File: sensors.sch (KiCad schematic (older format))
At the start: 11 parts

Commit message: Annotation
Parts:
- gave numbers to parts that had none: 11
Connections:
- net GND: no longer U4.17 (NC)
- no-connect marks 16 -> 17
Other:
- note added: "Ground distance sensor \n(Time of flight)"
- note added: "IMU 10dof"
- moved on the sheet: C19, C20, C21, C22, C23, C24, R16, R17, U4, U5, U6

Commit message: Change MCU to LQFP64 (instead of BGA)
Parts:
- added W3, W4, W5, W6, W7: TEST, symbol TEST
- U4: symbol MPU-9250 -> MPU-9250-RESCUE-speedy
- renumbered C19 to C15, C20 to C16, C21 to C17, C22 to C18, C23 to C19, C24 to C20, R16 to R15, R17 to R16
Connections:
- net MPU9250_CS: now also W6.2; no longer U4.22 (nCS)
- net MPU9250_INT: now also W7.2; no longer U4.12 (INT)
- net SPI1_MISO: now also W5.2; no longer U4.9 (AD0/SD0)
- net SPI1_MOSI: now also W4.2; no longer U4.24 (SDA/SDI)
- net SPI1_SCK: now also W3.2; no longer U4.23 (SCL/SCLK)
- net VCC: no longer C15.1, C16.1, C18.1, C19.1, C20.1, R15.1, R16.1, U4.13 (VDD), U4.8 (VDDIO), U5.1 (VDD), U5.2 (PS), U6.10 (AVDD), U6.8 (AVDD_VCSEL)
- new net: U4.12 (INT), W7.1
- new net: U4.22 (nCS), W6.1
- new net: U4.23 (SCL/SCLK), W3.1
- new net: U4.24 (SDA/SDI), W4.1
- new net: U4.9 (AD0/SD0), W5.1
- new net VCCA: C15.1, C16.1, C18.1, C19.1, C20.1, R15.1, R16.1, U4.13 (VDD), U4.8 (VDDIO), U5.1 (VDD), U5.2 (PS), U6.10 (AVDD), U6.8 (AVDD_VCSEL)
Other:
- moved on the sheet: C15, C16, C17, C18, U5

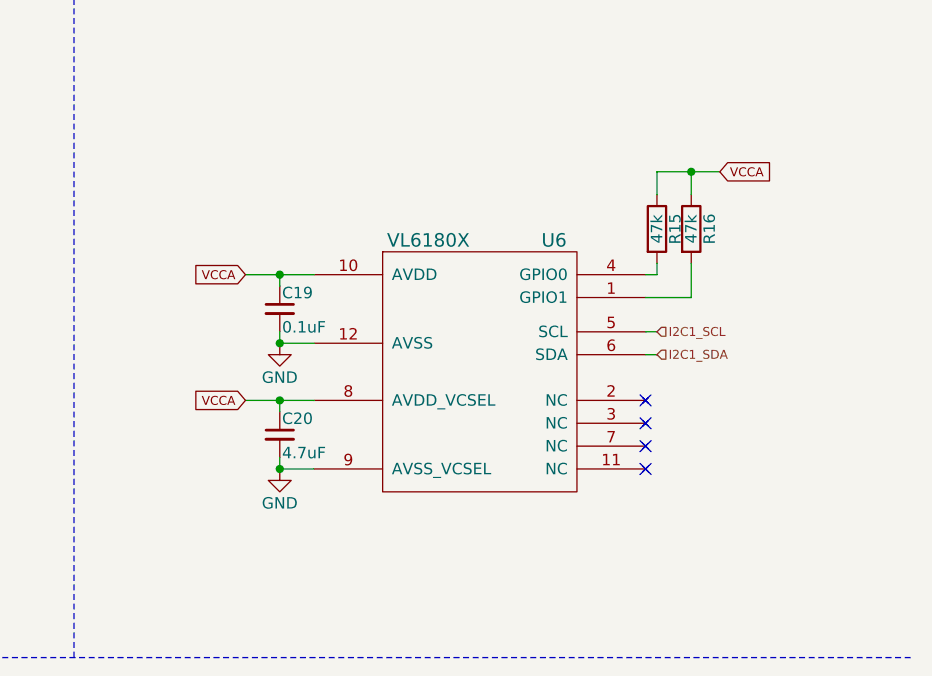
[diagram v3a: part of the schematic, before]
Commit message: Minor corrections
Wire GPIO of VL6180X to MCU
Remove UART4
Change Shottky diode
Add fuse on CAN bus power
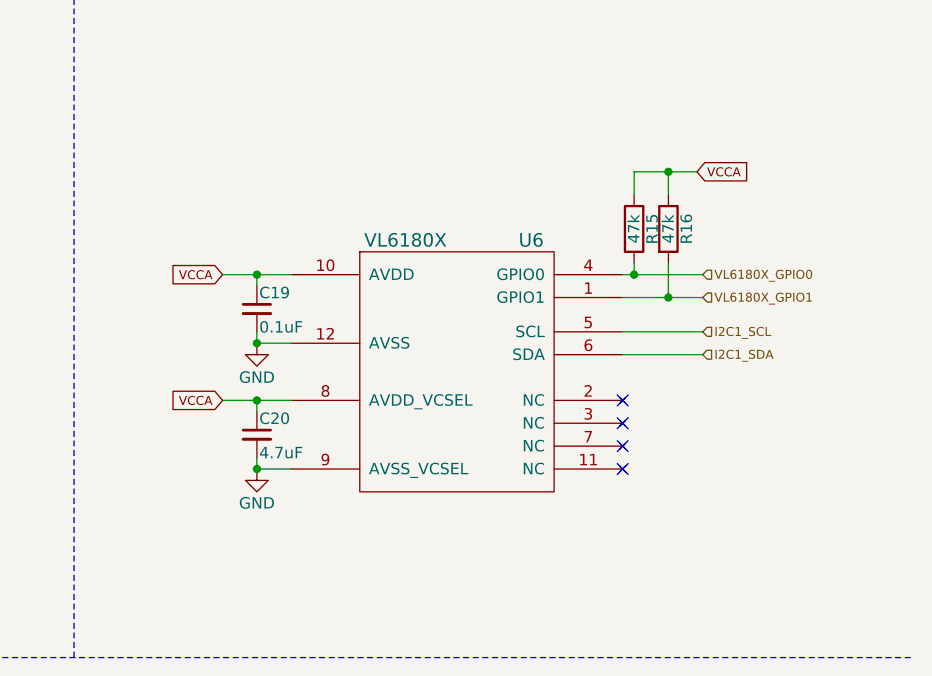
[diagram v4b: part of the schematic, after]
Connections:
- net VL6180X_GPIO0: now reaches R15.2, U6.4 (GPIO0)
- net VL6180X_GPIO1: now reaches R16.2, U6.1 (GPIO1)
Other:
- moved on the sheet: C19, C20, R15, R16, U6
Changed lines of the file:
@@
 $EndDescr
 $Comp
-L GND #PWR035
+L GND #PWR33
 U 1 1 5536D70F
 P 1275 2225
-F 0 "#PWR035" H 1275 1975 50  0001 C CNN
+F 0 "#PWR33" H 1275 1975 50  0001 C CNN
 F 1 "GND" H 1275 2075 50  0000 C CNN
 F 2 "" H 1275 2225 60  0000 C CNN
@@
 $EndComp
 $Comp
-L GND #PWR036
+L GND #PWR36
 U 1 1 5536D9F2
 P 3750 2975
-F 0 "#PWR036" H 3750 2725 50  0001 C CNN
+F 0 "#PWR36" H 3750 2725 50  0001 C CNN
 F 1 "GND" H 3750 2825 50  0000 C CNN
 F 2 "" H 3750 2975 60  0000 C CNN
@@
 NoConn ~ 3375 2875
 $Comp
-L VCC #PWR037
+L VCC #PWR34
 U 1 1 5536DF0C
 P 3525 3125
-F 0 "#PWR037" H 3525 2975 50  0001 C CNN
+F 0 "#PWR34" H 3525 2975 50  0001 C CNN
 F 1 "VCC" H 3525 3275 50  0000 C CNN
 F 2 "" H 3525 3125 60  0000 C CNN
@@
 $EndComp
 $Comp
-L GND #PWR038
+L GND #PWR35
 U 1 1 5536DF1F
 P 3525 3225
-F 0 "#PWR038" H 3525 2975 50  0001 C CNN
+F 0 "#PWR35" H 3525 2975 50  0001 C CNN
 F 1 "GND" H 3525 3075 50  0000 C CNN
 F 2 "" H 3525 3225 60  0000 C CNN
@@
 $EndComp
 $Comp
-L GND #PWR039
+L GND #PWR40
 U 1 1 5536FBED
-P 8450 3250
-F 0 "#PWR039" H 8450 3000 50  0001 C CNN
-F 1 "GND" H 8450 3100 50  0000 C CNN
-F 2 "" H 8450 3250 60  0000 C CNN
-F 3 "" H 8450 3250 60  0000 C CNN
-	1    8450 3250
-	1    0    0    -1
-$EndComp
-$Comp
-L GND #PWR040
+P 8350 3250
+F 0 "#PWR40" H 8350 3000 50  0001 C CNN
+F 1 "GND" H 8350 3100 50  0000 C CNN
+F 2 "" H 8350 3250 60  0000 C CNN
+F 3 "" H 8350 3250 60  0000 C CNN
+	1    8350 3250
+	1    0    0    -1
+$EndComp
+$Comp
+L GND #PWR39
 U 1 1 5536FC2A
-P 8450 2700
-F 0 "#PWR040" H 8450 2450 50  0001 C CNN
-F 1 "GND" H 8450 2550 50  0000 C CNN
-F 2 "" H 8450 2700 60  0000 C CNN
-F 3 "" H 8450 2700 60  0000 C CNN
-	1    8450 2700
+P 8350 2700
+F 0 "#PWR39" H 8350 2450 50  0001 C CNN
+F 1 "GND" H 8350 2550 50  0000 C CNN
+F 2 "" H 8350 2700 60  0000 C CNN
+F 3 "" H 8350 2700 60  0000 C CNN
+	1    8350 2700
 	1    0    0    -1
 $EndComp
@@
 L R R15
 U 1 1 5536FCF9
-P 10100 2200
-F 0 "R15" V 10180 2200 50  0000 C CNN
-F 1 "47k" V 10100 2200 50  0000 C CNN
-F 2 "" V 10030 2200 30  0000 C CNN
-F 3 "" H 10100 2200 30  0000 C CNN
-	1    10100 2200
+P 10000 2200
+F 0 "R15" V 10080 2200 50  0000 C CNN
+F 1 "47k" V 10000 2200 50  0000 C CNN
+F 2 "" V 9930 2200 30  0000 C CNN
+F 3 "" H 10000 2200 30  0000 C CNN
+	1    10000 2200
 	1    0    0    -1
 $EndComp
@@
 L R R16
 U 1 1 5536FD36
-P 10250 2200
-F 0 "R16" V 10330 2200 50  0000 C CNN
-F 1 "47k" V 10250 2200 50  0000 C CNN
-F 2 "" V 10180 2200 30  0000 C CNN
-F 3 "" H 10250 2200 30  0000 C CNN
-	1    10250 2200
+P 10150 2200
+F 0 "R16" V 10230 2200 50  0000 C CNN
+F 1 "47k" V 10150 2200 50  0000 C CNN
+F 2 "" V 10080 2200 30  0000 C CNN
+F 3 "" H 10150 2200 30  0000 C CNN
+	1    10150 2200
 	1    0    0    -1
 $EndComp
@@
 L VL6180X U6
 U 1 1 553709E6
-P 9000 2650
-F 0 "U6" H 9650 3050 59  0000 C CNN
-F 1 "VL6180X" H 9100 3050 59  0000 C CNN
-F 2 "" H 9200 3250 39  0000 C CNN
-F 3 "" H 9200 3250 39  0000 C CNN
-	1    9000 2650
+P 8900 2650
+F 0 "U6" H 9550 3050 59  0000 C CNN
+F 1 "VL6180X" H 9000 3050 59  0000 C CNN
+F 2 "" H 9100 3250 39  0000 C CNN
+F 3 "" H 9100 3250 39  0000 C CNN
+	1    8900 2650
 	1    0    0    -1
 $EndComp
@@
 $EndComp
 $Comp
-L GND #PWR041
+L GND #PWR37
 U 1 1 553864F8
 P 4975 2750
-F 0 "#PWR041" H 4975 2500 50  0001 C CNN
+F 0 "#PWR37" H 4975 2500 50  0001 C CNN
 F 1 "GND" H 4975 2600 50  0000 C CNN
 F 2 "" H 4975 2750 60  0000 C CNN
@@
 NoConn ~ 6725 2525
 $Comp
-L GND #PWR042
+L GND #PWR38
 U 1 1 55386A50
 P 6775 2775
-F 0 "#PWR042" H 6775 2525 50  0001 C CNN
+F 0 "#PWR38" H 6775 2525 50  0001 C CNN
 F 1 "GND" H 6775 2625 50  0000 C CNN
 F 2 "" H 6775 2775 60  0000 C CNN
@@
 	1    0    0    -1
 $EndComp
-NoConn ~ 10050 2950
-NoConn ~ 10050 3050
-NoConn ~ 10050 3150
-NoConn ~ 10050 3250
+NoConn ~ 9950 2950
+NoConn ~ 9950 3050
+NoConn ~ 9950 3150
+NoConn ~ 9950 3250
 NoConn ~ 1775 3125
 NoConn ~ 1775 3025
@@
 L C_Small C19
 U 1 1 55429127
-P 8450 2550
-F 0 "C19" H 8460 2620 50  0000 L CNN
-F 1 "0.1uF" H 8460 2470 50  0000 L CNN
-F 2 "" H 8450 2550 60  0000 C CNN
-F 3 "" H 8450 2550 60  0000 C CNN
-	1    8450 2550
+P 8350 2550
+F 0 "C19" H 8360 2620 50  0000 L CNN
+F 1 "0.1uF" H 8360 2470 50  0000 L CNN
+F 2 "" H 8350 2550 60  0000 C CNN
+F 3 "" H 8350 2550 60  0000 C CNN
+	1    8350 2550
 	1    0    0    -1
 $EndComp
@@
 L C_Small C20
 U 1 1 55429407
-P 8450 3100
-F 0 "C20" H 8460 3170 50  0000 L CNN
-F 1 "4.7uF" H 8460 3020 50  0000 L CNN
-F 2 "" H 8450 3100 60  0000 C CNN
-F 3 "" H 8450 3100 60  0000 C CNN
-	1    8450 3100
+P 8350 3100
+F 0 "C20" H 8360 3170 50  0000 L CNN
+F 1 "4.7uF" H 8360 3020 50  0000 L CNN
+F 2 "" H 8350 3100 60  0000 C CNN
+F 3 "" H 8350 3100 60  0000 C CNN
+	1    8350 3100
 	1    0    0    -1
 $EndComp
@@
 	3375 3125 3525 3125
 Wire Wire Line
-	8300 2950 8600 2950
-Wire Wire Line
-	8450 3250 8600 3250
-Connection ~ 8450 3250
-Connection ~ 8450 2950
-Wire Wire Line
-	10100 1950 10375 1950
-Wire Wire Line
-	10250 1950 10250 2050
-Wire Wire Line
-	10100 1950 10100 2050
-Connection ~ 10250 1950
-Wire Wire Line
-	10050 2400 10100 2400
-Wire Wire Line
-	10050 2500 10250 2500
-Wire Wire Line
-	10250 2500 10250 2350
-Wire Wire Line
-	10050 2650 10100 2650
-Wire Wire Line
-	10050 2750 10100 2750
-Wire Wire Line
-	10100 2400 10100 2350
-Wire Wire Line
-	8300 2400 8600 2400
+	8200 2950 8500 2950
+Wire Wire Line
+	8350 3250 8500 3250
+Connection ~ 8350 3250
+Connection ~ 8350 2950
+Wire Wire Line
+	10000 1950 10275 1950
+Wire Wire Line
+	10150 1950 10150 2050
+Wire Wire Line
+	10000 1950 10000 2050
+Connection ~ 10150 1950
+Wire Wire Line
+	9950 2400 10300 2400
+Wire Wire Line
+	9950 2500 10300 2500
+Wire Wire Line
+	10150 2500 10150 2350
+Wire Wire Line
+	9950 2650 10300 2650
+Wire Wire Line
+	9950 2750 10300 2750
+Wire Wire Line
+	10000 2400 10000 2350
+Wire Wire Line
+	8200 2400 8500 2400
 Wire Wire Line
 	4975 2675 4975 2750
@@
 Connection ~ 5175 2425
 Wire Wire Line
-	8600 2700 8450 2700
-Wire Wire Line
-	8450 2700 8450 2650
-Wire Wire Line
-	8450 2400 8450 2450
-Connection ~ 8450 2400
-Connection ~ 8450 2700
-Wire Wire Line
-	8450 3000 8450 2950
-Wire Wire Line
-	8450 3200 8450 3250
+	8500 2700 8350 2700
+Wire Wire Line
+	8350 2700 8350 2650
+Wire Wire Line
+	8350 2400 8350 2450
+Connection ~ 8350 2400
+Connection ~ 8350 2700
+Wire Wire Line
+	8350 3000 8350 2950
+Wire Wire Line
+	8350 3200 8350 3250
 Wire Notes Line
 	7550 4075 7550 500
@@
 Text HLabel 6775 2425 2    39   Input ~ 0
 I2C1_SDA
-Text HLabel 10100 2650 2    39   Input ~ 0
+Text HLabel 10300 2650 2    39   Input ~ 0
 I2C1_SCL
-Text HLabel 10100 2750 2    39   Input ~ 0
+Text HLabel 10300 2750 2    39   Input ~ 0
 I2C1_SDA
 NoConn ~ 1775 3225
@@
 Text GLabel 4975 2275 0    39   Input ~ 0
 VCCA
-Text GLabel 8300 2400 0    39   Input ~ 0
+Text GLabel 8200 2400 0    39   Input ~ 0
 VCCA
-Text GLabel 8300 2950 0    39   Input ~ 0
+Text GLabel 8200 2950 0    39   Input ~ 0
 VCCA
-Text GLabel 10375 1950 2    39   Input ~ 0
+Text GLabel 10275 1950 2    39   Input ~ 0
 VCCA
 $Comp
@@
 Wire Notes Line
 	475  4075 11225 4075
+Text HLabel 10300 2500 2    39   Input ~ 0
+VL6180X_GPIO1
+Text HLabel 10300 2400 2    39   Input ~ 0
+VL6180X_GPIO0
+Connection ~ 10000 2400
+Connection ~ 10150 2500
 $EndSCHEMATC

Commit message: Netlist
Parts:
- C15, C16, C17, C18, C19, C20, R15, R16: footprint (none) -> _std:_0402
- U4: footprint (none) -> Housings_DFN_QFN:QFN-24-1EP_3x3mm_Pitch0.4mm
- U5: footprint MODULE -> _sensors:_MS5611-01BA
- U6: footprint (none) -> _sensors:VL6180X
- W3, W4, W5, W6, W7: footprint (none) -> Measurement_Points:Measurement_Point_Square-SMD-Pad_Small
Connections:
- net VL6180X_GPIO0: no longer names the net of R15.2, U6.4 (GPIO0)
- net VL6180X_GPIO1: no longer names the net of R16.2, U6.1 (GPIO1)
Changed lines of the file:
@@
 $EndDescr
 $Comp
-L GND #PWR33
+L GND #PWR033
 U 1 1 5536D70F
 P 1275 2225
-F 0 "#PWR33" H 1275 1975 50  0001 C CNN
+F 0 "#PWR033" H 1275 1975 50  0001 C CNN
 F 1 "GND" H 1275 2075 50  0000 C CNN
 F 2 "" H 1275 2225 60  0000 C CNN
@@
 $EndComp
 $Comp
-L GND #PWR36
+L GND #PWR034
 U 1 1 5536D9F2
 P 3750 2975
-F 0 "#PWR36" H 3750 2725 50  0001 C CNN
+F 0 "#PWR034" H 3750 2725 50  0001 C CNN
 F 1 "GND" H 3750 2825 50  0000 C CNN
 F 2 "" H 3750 2975 60  0000 C CNN
@@
 NoConn ~ 3375 2875
 $Comp
-L VCC #PWR34
+L VCC #PWR035
 U 1 1 5536DF0C
 P 3525 3125
-F 0 "#PWR34" H 3525 2975 50  0001 C CNN
+F 0 "#PWR035" H 3525 2975 50  0001 C CNN
 F 1 "VCC" H 3525 3275 50  0000 C CNN
 F 2 "" H 3525 3125 60  0000 C CNN
@@
 $EndComp
 $Comp
-L GND #PWR35
+L GND #PWR036
 U 1 1 5536DF1F
 P 3525 3225
-F 0 "#PWR35" H 3525 2975 50  0001 C CNN
+F 0 "#PWR036" H 3525 2975 50  0001 C CNN
 F 1 "GND" H 3525 3075 50  0000 C CNN
 F 2 "" H 3525 3225 60  0000 C CNN
@@
 $EndComp
 $Comp
-L GND #PWR40
+L GND #PWR037
 U 1 1 5536FBED
 P 8350 3250
-F 0 "#PWR40" H 8350 3000 50  0001 C CNN
+F 0 "#PWR037" H 8350 3000 50  0001 C CNN
 F 1 "GND" H 8350 3100 50  0000 C CNN
 F 2 "" H 8350 3250 60  0000 C CNN
@@
 $EndComp
 $Comp
-L GND #PWR39
+L GND #PWR038
 U 1 1 5536FC2A
 P 8350 2700
-F 0 "#PWR39" H 8350 2450 50  0001 C CNN
+F 0 "#PWR038" H 8350 2450 50  0001 C CNN
 F 1 "GND" H 8350 2550 50  0000 C CNN
 F 2 "" H 8350 2700 60  0000 C CNN
@@
 F 0 "R15" V 10080 2200 50  0000 C CNN
 F 1 "47k" V 10000 2200 50  0000 C CNN
-F 2 "" V 9930 2200 30  0000 C CNN
+F 2 "_std:_0402" V 9930 2200 30  0001 C CNN
 F 3 "" H 10000 2200 30  0000 C CNN
 	1    10000 2200
@@
 F 0 "R16" V 10230 2200 50  0000 C CNN
 F 1 "47k" V 10150 2200 50  0000 C CNN
-F 2 "" V 10080 2200 30  0000 C CNN
+F 2 "_std:_0402" V 10080 2200 30  0001 C CNN
 F 3 "" H 10150 2200 30  0000 C CNN
 	1    10150 2200
@@
 F 0 "U6" H 9550 3050 59  0000 C CNN
 F 1 "VL6180X" H 9000 3050 59  0000 C CNN
-F 2 "" H 9100 3250 39  0000 C CNN
+F 2 "_sensors:VL6180X" H 9100 3250 39  0001 C CNN
 F 3 "" H 9100 3250 39  0000 C CNN
 	1    8900 2650
@@
 F 0 "U5" H 6325 2925 50  0000 C CNN
 F 1 "MS5611-01BA" H 5825 2925 50  0000 C CNN
-F 2 "MODULE" H 5975 2525 50  0001 C CNN
+F 2 "_sensors:_MS5611-01BA" H 5975 2525 50  0001 C CNN
 F 3 "DOCUMENTATION" H 5975 2525 50  0001 C CNN
 	1    5975 2525
@@
 $EndComp
 $Comp
-L GND #PWR37
+L GND #PWR039
 U 1 1 553864F8
 P 4975 2750
-F 0 "#PWR37" H 4975 2500 50  0001 C CNN
+F 0 "#PWR039" H 4975 2500 50  0001 C CNN
 F 1 "GND" H 4975 2600 50  0000 C CNN
 F 2 "" H 4975 2750 60  0000 C CNN
@@
 NoConn ~ 6725 2525
 $Comp
-L GND #PWR38
+L GND #PWR040
 U 1 1 55386A50
 P 6775 2775
-F 0 "#PWR38" H 6775 2525 50  0001 C CNN
+F 0 "#PWR040" H 6775 2525 50  0001 C CNN
 F 1 "GND" H 6775 2625 50  0000 C CNN
 F 2 "" H 6775 2775 60  0000 C CNN
@@
 F 0 "U4" H 2975 3325 60  0000 C CNN
 F 1 "MPU-9250" H 2325 3325 60  0000 C CNN
-F 2 "" H 2575 3125 60  0000 C CNN
+F 2 "Housings_DFN_QFN:QFN-24-1EP_3x3mm_Pitch0.4mm" H 2575 3125 60  0001 C CNN
 F 3 "" H 2575 3125 60  0000 C CNN
 	1    2575 2525
@@
 F 0 "C15" H 1285 2095 50  0000 L CNN
 F 1 "0.1uF" H 1285 1945 50  0000 L CNN
-F 2 "" H 1275 2025 60  0000 C CNN
+F 2 "_std:_0402" H 1275 2025 60  0001 C CNN
 F 3 "" H 1275 2025 60  0000 C CNN
 	1    1275 2025
@@
 F 0 "C16" H 1535 2095 50  0000 L CNN
 F 1 "10nF" H 1535 1945 50  0000 L CNN
-F 2 "" H 1525 2025 60  0000 C CNN
+F 2 "_std:_0402" H 1525 2025 60  0001 C CNN
 F 3 "" H 1525 2025 60  0000 C CNN
 	1    1525 2025
@@
 F 0 "C17" H 3760 2945 50  0000 L CNN
 F 1 "0.1uF" H 3760 2795 50  0000 L CNN
-F 2 "" H 3750 2875 60  0000 C CNN
+F 2 "_std:_0402" H 3750 2875 60  0001 C CNN
 F 3 "" H 3750 2875 60  0000 C CNN
 	1    3750 2875
@@
 F 0 "C18" H 4985 2645 50  0000 L CNN
 F 1 "0.1uF" H 4985 2495 50  0000 L CNN
-F 2 "" H 4975 2575 60  0000 C CNN
+F 2 "_std:_0402" H 4975 2575 60  0001 C CNN
 F 3 "" H 4975 2575 60  0000 C CNN
 	1    4975 2575
@@
 F 0 "C19" H 8360 2620 50  0000 L CNN
 F 1 "0.1uF" H 8360 2470 50  0000 L CNN
-F 2 "" H 8350 2550 60  0000 C CNN
+F 2 "_std:_0402" H 8350 2550 60  0001 C CNN
 F 3 "" H 8350 2550 60  0000 C CNN
 	1    8350 2550
@@
 F 0 "C20" H 8360 3170 50  0000 L CNN
 F 1 "4.7uF" H 8360 3020 50  0000 L CNN
-F 2 "" H 8350 3100 60  0000 C CNN
+F 2 "_std:_0402" H 8350 3100 60  0001 C CNN
 F 3 "" H 8350 3100 60  0000 C CNN
 	1    8350 3100
@@
 	10000 1950 10000 2050
 Connection ~ 10150 1950
-Wire Wire Line
-	9950 2400 10300 2400
-Wire Wire Line
-	9950 2500 10300 2500
 Wire Wire Line
 	10150 2500 10150 2350
@@
 F 0 "W3" H 3725 2150 40  0000 C CNN
 F 1 "TEST" H 3575 2125 20  0000 C CNN
-F 2 "" H 3575 2125 60  0000 C CNN
+F 2 "Measurement_Points:Measurement_Point_Square-SMD-Pad_Small" H 3575 2125 60  0001 C CNN
 F 3 "" H 3575 2125 60  0000 C CNN
 	1    3575 2125
@@
 F 0 "W4" H 3725 2250 40  0000 C CNN
 F 1 "TEST" H 3575 2225 20  0000 C CNN
-F 2 "" H 3575 2225 60  0000 C CNN
+F 2 "Measurement_Points:Measurement_Point_Square-SMD-Pad_Small" H 3575 2225 60  0001 C CNN
 F 3 "" H 3575 2225 60  0000 C CNN
 	1    3575 2225
@@
 F 0 "W5" H 3725 2400 40  0000 C CNN
 F 1 "TEST" H 3575 2375 20  0000 C CNN
-F 2 "" H 3575 2375 60  0000 C CNN
+F 2 "Measurement_Points:Measurement_Point_Square-SMD-Pad_Small" H 3575 2375 60  0001 C CNN
 F 3 "" H 3575 2375 60  0000 C CNN
 	1    3575 2375
@@
 F 0 "W6" H 3725 2550 40  0000 C CNN
 F 1 "TEST" H 3575 2525 20  0000 C CNN
-F 2 "" H 3575 2525 60  0000 C CNN
+F 2 "Measurement_Points:Measurement_Point_Square-SMD-Pad_Small" H 3575 2525 60  0001 C CNN
 F 3 "" H 3575 2525 60  0000 C CNN
 	1    3575 2525
@@
 F 0 "W7" H 3725 2700 40  0000 C CNN
 F 1 "TEST" H 3575 2675 20  0000 C CNN
-F 2 "" H 3575 2675 60  0000 C CNN
+F 2 "Measurement_Points:Measurement_Point_Square-SMD-Pad_Small" H 3575 2675 60  0001 C CNN
 F 3 "" H 3575 2675 60  0000 C CNN
 	1    3575 2675
@@
 Wire Notes Line
 	475  4075 11225 4075
-Text HLabel 10300 2500 2    39   Input ~ 0
-VL6180X_GPIO1
-Text HLabel 10300 2400 2    39   Input ~ 0
-VL6180X_GPIO0
-Connection ~ 10000 2400
-Connection ~ 10150 2500
+Wire Wire Line
+	9950 2400 10000 2400
+Wire Wire Line
+	9950 2500 10150 2500
 $EndSCHEMATC

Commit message: Remove CAN interface
(not useful enough, takes too much place)
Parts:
- W3, W4, W5, W6, W7: footprint Measurement_Points:Measurement_Point_Square-SMD-Pad_Small -> _std:Measurement_Point_Round-SMD-Pad_Small
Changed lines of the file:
@@
 F 0 "W3" H 3725 2150 40  0000 C CNN
 F 1 "TEST" H 3575 2125 20  0000 C CNN
-F 2 "Measurement_Points:Measurement_Point_Square-SMD-Pad_Small" H 3575 2125 60  0001 C CNN
+F 2 "_std:Measurement_Point_Round-SMD-Pad_Small" H 3575 2125 60  0001 C CNN
 F 3 "" H 3575 2125 60  0000 C CNN
 	1    3575 2125
@@
 F 0 "W4" H 3725 2250 40  0000 C CNN
 F 1 "TEST" H 3575 2225 20  0000 C CNN
-F 2 "Measurement_Points:Measurement_Point_Square-SMD-Pad_Small" H 3575 2225 60  0001 C CNN
+F 2 "_std:Measurement_Point_Round-SMD-Pad_Small" H 3575 2225 60  0001 C CNN
 F 3 "" H 3575 2225 60  0000 C CNN
 	1    3575 2225
@@
 F 0 "W5" H 3725 2400 40  0000 C CNN
 F 1 "TEST" H 3575 2375 20  0000 C CNN
-F 2 "Measurement_Points:Measurement_Point_Square-SMD-Pad_Small" H 3575 2375 60  0001 C CNN
+F 2 "_std:Measurement_Point_Round-SMD-Pad_Small" H 3575 2375 60  0001 C CNN
 F 3 "" H 3575 2375 60  0000 C CNN
 	1    3575 2375
@@
 F 0 "W6" H 3725 2550 40  0000 C CNN
 F 1 "TEST" H 3575 2525 20  0000 C CNN
-F 2 "Measurement_Points:Measurement_Point_Square-SMD-Pad_Small" H 3575 2525 60  0001 C CNN
+F 2 "_std:Measurement_Point_Round-SMD-Pad_Small" H 3575 2525 60  0001 C CNN
 F 3 "" H 3575 2525 60  0000 C CNN
 	1    3575 2525
@@
 F 0 "W7" H 3725 2700 40  0000 C CNN
 F 1 "TEST" H 3575 2675 20  0000 C CNN
-F 2 "Measurement_Points:Measurement_Point_Square-SMD-Pad_Small" H 3575 2675 60  0001 C CNN
+F 2 "_std:Measurement_Point_Round-SMD-Pad_Small" H 3575 2675 60  0001 C CNN
 F 3 "" H 3575 2675 60  0000 C CNN
 	1    3575 2675

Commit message: Regenerate netlist & Start placing footprints
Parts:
- removed W3, W4, W5, W6, W7: TEST, _std:Measurement_Point_Round-SMD-Pad_Small, symbol TEST
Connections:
- net MPU9250_CS: now also U4.22 (nCS)
- net MPU9250_INT: now also U4.12 (INT)
- net SPI1_MISO: now also U4.9 (AD0/SD0)
- net SPI1_MOSI: now also U4.24 (SDA/SDI)
- net SPI1_SCK: now also U4.23 (SCL/SCLK)
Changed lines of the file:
@@
 EESchema Schematic File Version 2
-LIBS:speedy-rescue
 LIBS:speedy-cache
 LIBS:power
@@
 	1    0    0    -1
 $EndComp
-Text HLabel 3825 2125 2    39   Input ~ 0
+Text HLabel 3425 2125 2    39   Input ~ 0
 SPI1_SCK
-Text HLabel 3825 2225 2    39   Input ~ 0
+Text HLabel 3425 2225 2    39   Input ~ 0
 SPI1_MOSI
-Text HLabel 3825 2375 2    39   Input ~ 0
+Text HLabel 3425 2375 2    39   Input ~ 0
 SPI1_MISO
-Text HLabel 3825 2525 2    39   Input ~ 0
+Text HLabel 3425 2525 2    39   Input ~ 0
 MPU9250_CS
-Text HLabel 3825 2675 2    39   Input ~ 0
+Text HLabel 3425 2675 2    39   Input ~ 0
 MPU9250_INT
 $Comp
@@
 	3750 2775 3375 2775
 Wire Wire Line
-	3825 2375 3775 2375
-Wire Wire Line
-	3825 2525 3775 2525
-Wire Wire Line
-	3825 2225 3775 2225
-Wire Wire Line
-	3825 2125 3775 2125
-Wire Wire Line
-	3825 2675 3775 2675
+	3425 2375 3375 2375
+Wire Wire Line
+	3425 2525 3375 2525
+Wire Wire Line
+	3425 2225 3375 2225
+Wire Wire Line
+	3425 2125 3375 2125
+Wire Wire Line
+	3425 2675 3375 2675
 Wire Wire Line
 	3525 3225 3375 3225
@@
 Text GLabel 10275 1950 2    39   Input ~ 0
 VCCA
-$Comp
-L TEST W3
-U 1 1 55799AAF
-P 3575 2125
-F 0 "W3" H 3725 2150 40  0000 C CNN
-F 1 "TEST" H 3575 2125 20  0000 C CNN
-F 2 "_std:Measurement_Point_Round-SMD-Pad_Small" H 3575 2125 60  0001 C CNN
-F 3 "" H 3575 2125 60  0000 C CNN
-	1    3575 2125
-	1    0    0    -1
-$EndComp
-$Comp
-L TEST W4
-U 1 1 55799BD9
-P 3575 2225
-F 0 "W4" H 3725 2250 40  0000 C CNN
-F 1 "TEST" H 3575 2225 20  0000 C CNN
-F 2 "_std:Measurement_Point_Round-SMD-Pad_Small" H 3575 2225 60  0001 C CNN
-F 3 "" H 3575 2225 60  0000 C CNN
-	1    3575 2225
-	1    0    0    -1
-$EndComp
-$Comp
-L TEST W5
-U 1 1 55799C09
-P 3575 2375
-F 0 "W5" H 3725 2400 40  0000 C CNN
-F 1 "TEST" H 3575 2375 20  0000 C CNN
-F 2 "_std:Measurement_Point_Round-SMD-Pad_Small" H 3575 2375 60  0001 C CNN
-F 3 "" H 3575 2375 60  0000 C CNN
-	1    3575 2375
-	1    0    0    -1
-$EndComp
-$Comp
-L TEST W6
-U 1 1 55799C3F
-P 3575 2525
-F 0 "W6" H 3725 2550 40  0000 C CNN
-F 1 "TEST" H 3575 2525 20  0000 C CNN
-F 2 "_std:Measurement_Point_Round-SMD-Pad_Small" H 3575 2525 60  0001 C CNN
-F 3 "" H 3575 2525 60  0000 C CNN
-	1    3575 2525
-	1    0    0    -1
-$EndComp
-$Comp
-L TEST W7
-U 1 1 55799C79
-P 3575 2675
-F 0 "W7" H 3725 2700 40  0000 C CNN
-F 1 "TEST" H 3575 2675 20  0000 C CNN
-F 2 "_std:Measurement_Point_Round-SMD-Pad_Small" H 3575 2675 60  0001 C CNN
-F 3 "" H 3575 2675 60  0000 C CNN
-	1    3575 2675
-	1    0    0    -1
-$EndComp
 Wire Notes Line
 	475  4075 11225 4075
